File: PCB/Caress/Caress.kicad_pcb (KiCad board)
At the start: 2 copper layers, 60 x 110 mm, 24 parts, among them J1 Conn_01x04_Male_Cell, J10 Conn_01x01_Male, J11 Conn_01x01_Male, J12 Conn_01x01_Male, J13 Conn_01x01_Male, J2 Conn_01x01_Male, J3 Conn_01x01_Male, J4 Conn_01x03_Male_AX12A, J5 Conn_01x02_Male_12V, J6 Conn_01x01_Male, J7 Conn_01x01_Male, J8 Conn_01x01_Male, J9 Conn_01x01_Male, U1 SEN-13879, U2 SN74LS241N, U3 L7805, U4 WRL-00691

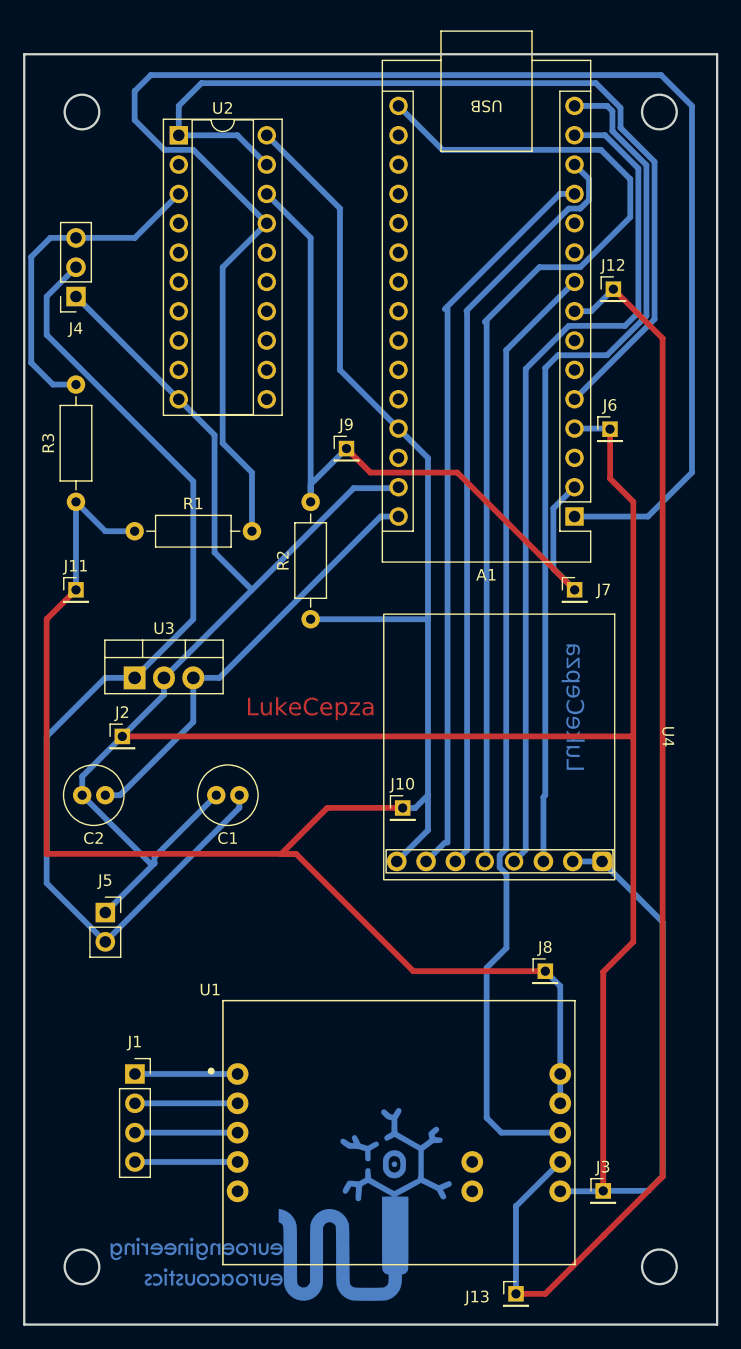
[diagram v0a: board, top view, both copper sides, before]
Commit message: Updated PCB files; added desing files for caress and vibration
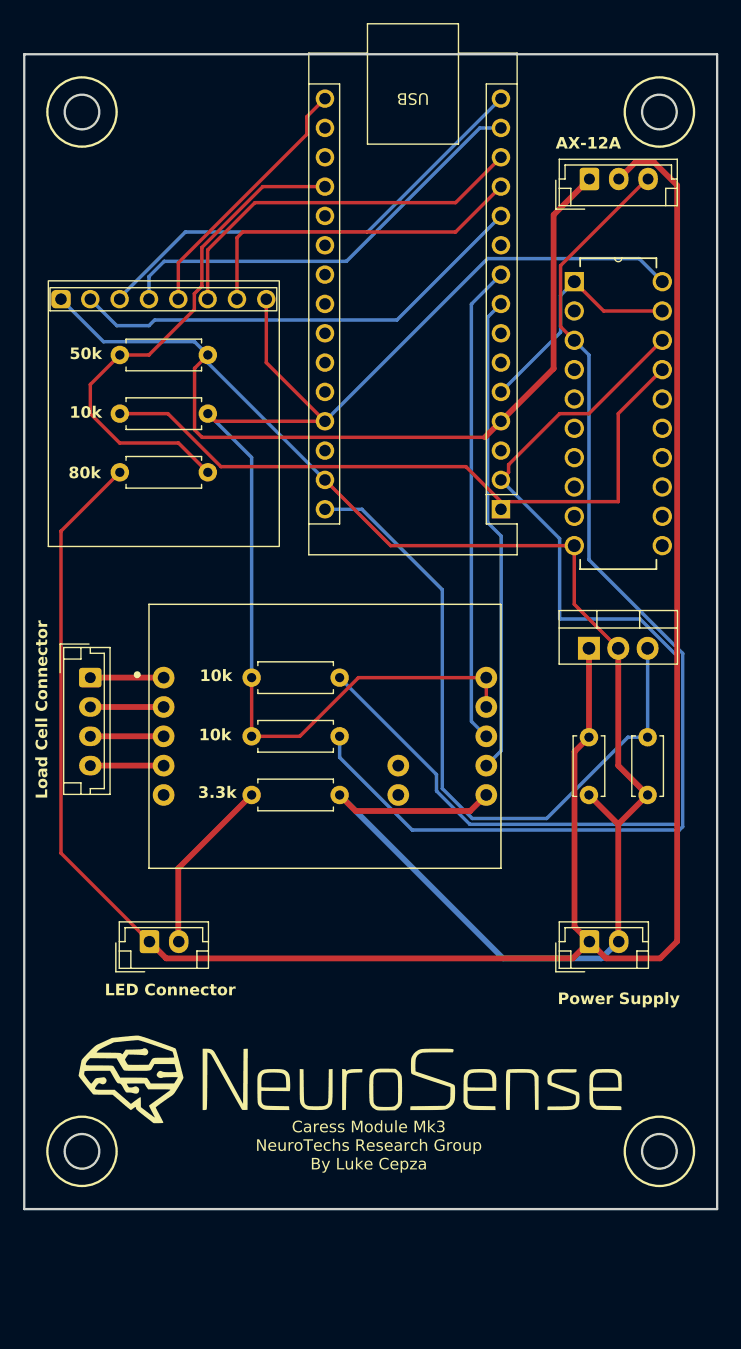
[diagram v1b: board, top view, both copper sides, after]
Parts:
- removed the G*** at (62.3, 139.7)
- removed J10, J11, J12, J13, J6, J7, J8, J9: Conn_01x01_Male, Connector_PinHeader_2.00mm:PinHeader_1x01_P2.00mm_Vertical
- removed J5: Conn_01x02_Male_12V, Connector_PinSocket_2.54mm:PinSocket_1x02_P2.54mm_Vertical
- added G***: LOGO, Logo:NeuroSenseLogo50mm, F.Cu at (68.6, 128.5)
- added R4: 10k, Resistor_THT:R_Axial_DIN0207_L6.3mm_D2.5mm_P7.62mm_Horizontal, F.Cu at (55.9, 71.1)
- added R5: 10k, Resistor_THT:R_Axial_DIN0207_L6.3mm_D2.5mm_P7.62mm_Horizontal, F.Cu at (59.7, 94.0)
- added R6: 10k, Resistor_THT:R_Axial_DIN0207_L6.3mm_D2.5mm_P7.62mm_Horizontal, F.Cu at (59.7, 99.1)
- C1: value 220uF -> 33uF; footprint Capacitor_THT:C_Radial_D5.0mm_H11.0mm_P2.00mm -> Capacitor_THT:C_Disc_D5.0mm_W2.5mm_P5.00mm
- C2: footprint Capacitor_THT:C_Radial_D5.0mm_H11.0mm_P2.00mm -> Capacitor_THT:C_Disc_D5.0mm_W2.5mm_P5.00mm
- J1: value Conn_01x04_Male_Cell -> LoadCellConnector; footprint Connector_PinSocket_2.54mm:PinSocket_1x04_P2.54mm_Vertical -> Connector_JST:JST_EH_B4B-EH-A_1x04_P2.50mm_Vertical
- J2: value Conn_01x01_Male -> Conn_01x02_Pin; footprint Connector_PinHeader_2.00mm:PinHeader_1x01_P2.00mm_Vertical -> Connector_JST:JST_EH_B2B-EH-A_1x02_P2.50mm_Vertical
- J3: value Conn_01x01_Male -> Conn_01x02_Male; footprint Connector_PinHeader_2.00mm:PinHeader_1x01_P2.00mm_Vertical -> Connector_JST:JST_EH_B2B-EH-A_1x02_P2.50mm_Vertical
- J4: value Conn_01x03_Male_AX12A -> Conn_AX12A; footprint Connector_PinSocket_2.54mm:PinSocket_1x03_P2.54mm_Vertical -> Connector_JST:JST_EH_B3B-EH-A_1x03_P2.50mm_Vertical
- R1: value 10k -> 80k; footprint Resistor_THT:R_Axial_DIN0207_L6.3mm_D2.5mm_P10.16mm_Horizontal -> Resistor_THT:R_Axial_DIN0207_L6.3mm_D2.5mm_P7.62mm_Horizontal
- R2: value 10k -> 50K; footprint Resistor_THT:R_Axial_DIN0207_L6.3mm_D2.5mm_P10.16mm_Horizontal -> Resistor_THT:R_Axial_DIN0207_L6.3mm_D2.5mm_P7.62mm_Horizontal
- R3: value 10k -> 3.3k; footprint Resistor_THT:R_Axial_DIN0207_L6.3mm_D2.5mm_P10.16mm_Horizontal -> Resistor_THT:R_Axial_DIN0207_L6.3mm_D2.5mm_P7.62mm_Horizontal
- U1: value SEN-13879 -> WRL-00691; footprint SEN-13879:SPARKFUN_SEN-13879 -> Mods:WRL-00691
- U2: value SN74LS241N -> SEN-13879; footprint Package_DIP:DIP-20_W7.62mm_Socket -> Mods:SPARKFUN_SEN-13879
- U3: value L7805 -> LM7805_TO220
- U4: value WRL-00691 -> SN74LS241N; footprint SEN-13879:WRL-00691 -> Mods:DIP254P762X508-20
- moved U1 70.3 mm to (43.0, 69.5), turned to 90 degrees
- moved U2 53.6 mm to (66.0, 99.1)
- moved C2 47.2 mm to (94.0, 99.1), turned to -90 degrees
- moved J4 45.6 mm to (88.9, 50.8), turned to 0 degrees
- moved U3 39.4 mm to (88.9, 91.4)
- moved J1 34.5 mm to (45.7, 94.0), turned to -90 degrees
- moved C1 30.7 mm to (88.9, 99.1), turned to -90 degrees
- moved R3 29.6 mm to (59.7, 104.1), turned to 0 degrees
- moved R2 28.2 mm to (48.3, 66.0), turned to 0 degrees
- moved J3 21.6 mm to (88.9, 116.8)
- moved U4 19.7 mm to (95.2, 82.5), turned to 0 degrees
- moved J2 17.9 mm to (50.8, 116.8)
- moved A1 6.40 mm to (81.3, 79.4)
- moved R1 5.26 mm to (48.3, 76.2)
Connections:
- net Net-(A1-Pad30) renamed /VIN_5v
- A1 pad 1: Net-(A1-Pad1) -> /D1_2A4
- A1 pad 11: unconnected-(A1-Pad11) -> /D8_IRQ
- A1 pad 12: Net-(A1-Pad12) -> /D9_CE
- A1 pad 13: Net-(A1-Pad13) -> /D10_CSN
- A1 pad 14: Net-(A1-Pad14) -> /D11_MOSI
- A1 pad 15: Net-(A1-Pad15) -> /D12_MISO
- A1 pad 16: Net-(A1-Pad16) -> /D13_SCK
- A1 pad 19: unconnected-(A1-Pad19) -> /A0_VBat
- A1 pad 2: Net-(A1-Pad2) -> /D0_1Y1
- A1 pad 5: Net-(A1-Pad5) -> /D2_G
- A1 pad 8: Net-(A1-Pad8) -> /D5_CLK
- A1 pad 9: Net-(A1-Pad9) -> /D6_DAT
- J1 pad 1: Net-(J1-Pad1) -> Net-(J1-Pin_1)
- J1 pad 2: Net-(J1-Pad2) -> Net-(J1-Pin_2)
- J1 pad 3: Net-(J1-Pad3) -> Net-(J1-Pin_3)
- J1 pad 4: Net-(J1-Pad4) -> Net-(J1-Pin_4)
- J2 pad 1: GND -> +12V
- J3 pad 1: GND -> +12V
- J4 pad 3: Net-(J4-Pad3) -> Net-(J4-Pin_3)
- R1 pad 1: +5V -> +12V
- R1 pad 2: Net-(A1-Pad1) -> /A0_VBat
- R2 pad 1: +5V -> /A0_VBat
- R2 pad 2: Net-(A1-Pad2) -> GND
- R3 pad 1: +5V -> Net-(J2-Pin_2)
- R3 pad 2: Net-(J4-Pad3) -> GND
- U1 pad 1: Net-(J1-Pad1) -> GND
- U1 pad 2: Net-(J1-Pad2) -> /D8_IRQ
- U1 pad 3: Net-(J1-Pad3) -> /D12_MISO
- U1 pad 4: Net-(J1-Pad4) -> /D11_MOSI
- U1 pad 5: unconnected-(U1-Pad5) -> /D13_SCK
- U1 pad 6: GND -> /D10_CSN
- U1 pad 7: Net-(A1-Pad8) -> /D9_CE
- U1 pad 8: Net-(A1-Pad9) -> +5V
- U2 pad 1: Net-(A1-Pad5) -> Net-(J1-Pin_1)
- U2 pad 10: GND -> +5V
- U2 pad 2: unconnected-(U2-Pad2) -> Net-(J1-Pin_2)
- U2 pad 3: Net-(J4-Pad3) -> Net-(J1-Pin_3)
- U2 pad 4: unconnected-(U2-Pad4) -> Net-(J1-Pin_4)
- U2 pad 6: unconnected-(U2-Pad6) -> GND
- U2 pad 7: unconnected-(U2-Pad7) -> /D5_CLK
- U2 pad 8: unconnected-(U2-Pad8) -> /D6_DAT
- U2 pad 9: unconnected-(U2-Pad9) -> +5V
- U4 pad 1: GND -> /D2_G
- U4 pad 2: GND -> unconnected-(U4-1A1-Pad2)
- U4 pad 3: Net-(A1-Pad15) -> Net-(J4-Pin_3)
- U4 pad 4: Net-(A1-Pad14) -> unconnected-(U4-1A2-Pad4)
- U4 pad 5: Net-(A1-Pad16) -> unconnected-(U4-2Y3-Pad5)
- U4 pad 6: Net-(A1-Pad13) -> unconnected-(U4-1A3-Pad6)
- U4 pad 7: Net-(A1-Pad12) -> unconnected-(U4-2Y2-Pad7)
- U4 pad 8: +5V -> unconnected-(U4-1A4-Pad8)
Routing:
- net Net-(A1-Pad1): track 140.4 -> 0.00 mm
- net Net-(A1-Pad8): track 112.7 -> 0.00 mm
- net +12V: track 91.1 -> 192.4 mm
- net Net-(J4-Pin_3): track 0.00 -> 97.8 mm
- net /D0_1Y1: track 0.00 -> 94.9 mm
- net Net-(A1-Pad16): track 89.8 -> 0.00 mm
- net Net-(A1-Pad9): track 82.9 -> 0.00 mm
- net Net-(A1-Pad5): track 80.5 -> 0.00 mm
- net +5V: track 193.4 -> 113.4 mm
- net Net-(A1-Pad15): track 75.8 -> 0.00 mm
- net Net-(A1-Pad14): track 74.0 -> 0.00 mm
- net Net-(A1-Pad2): track 69.7 -> 0.00 mm
- net Net-(A1-Pad13): track 66.2 -> 0.00 mm
- net Net-(A1-Pad12): track 63.9 -> 0.00 mm
- net /D1_2A4: track 0.00 -> 60.3 mm
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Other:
- board size 60 x 110 mm -> 60 x 100 mm
- board text added: "10k"
- board text added: "3.3k"
- board text added: "50k"
- board text added: "80k"
- board text added: "AX-12A"
- board text added: "Caress Module Mk3 NeuroTechs Research Group By Luke Cepza"
- board text added: "LED Connector"
- board text added: "Load Cell Connector"
- board text added: "Power Supply"
- board text removed: "LukeCepza"
